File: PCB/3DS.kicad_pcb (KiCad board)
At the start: 2 copper layers, 12 x 40.6 mm, 8 parts, among them J1 3DS Joystick Pads, U1 ATtiny45V-10SU

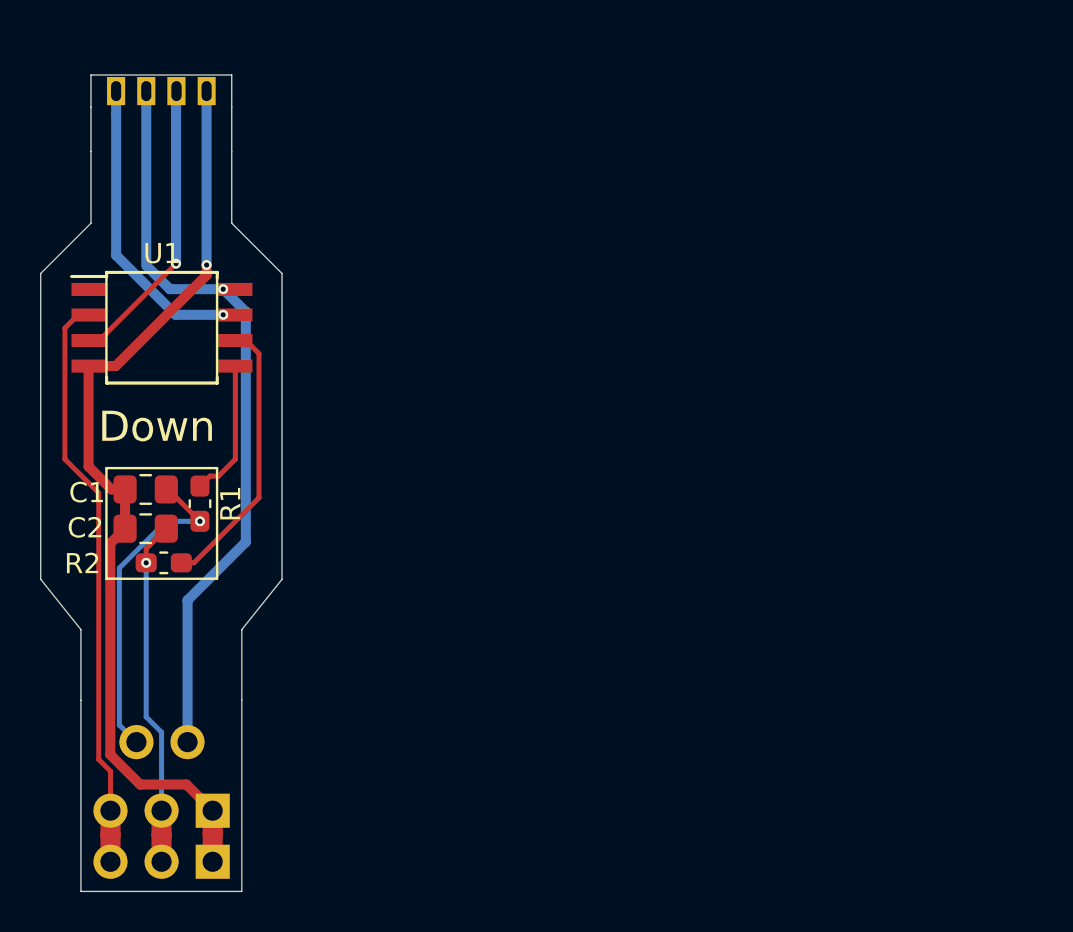
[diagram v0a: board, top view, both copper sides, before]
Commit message: Moved from flex PCB to a roughed-out fiberglass PCB
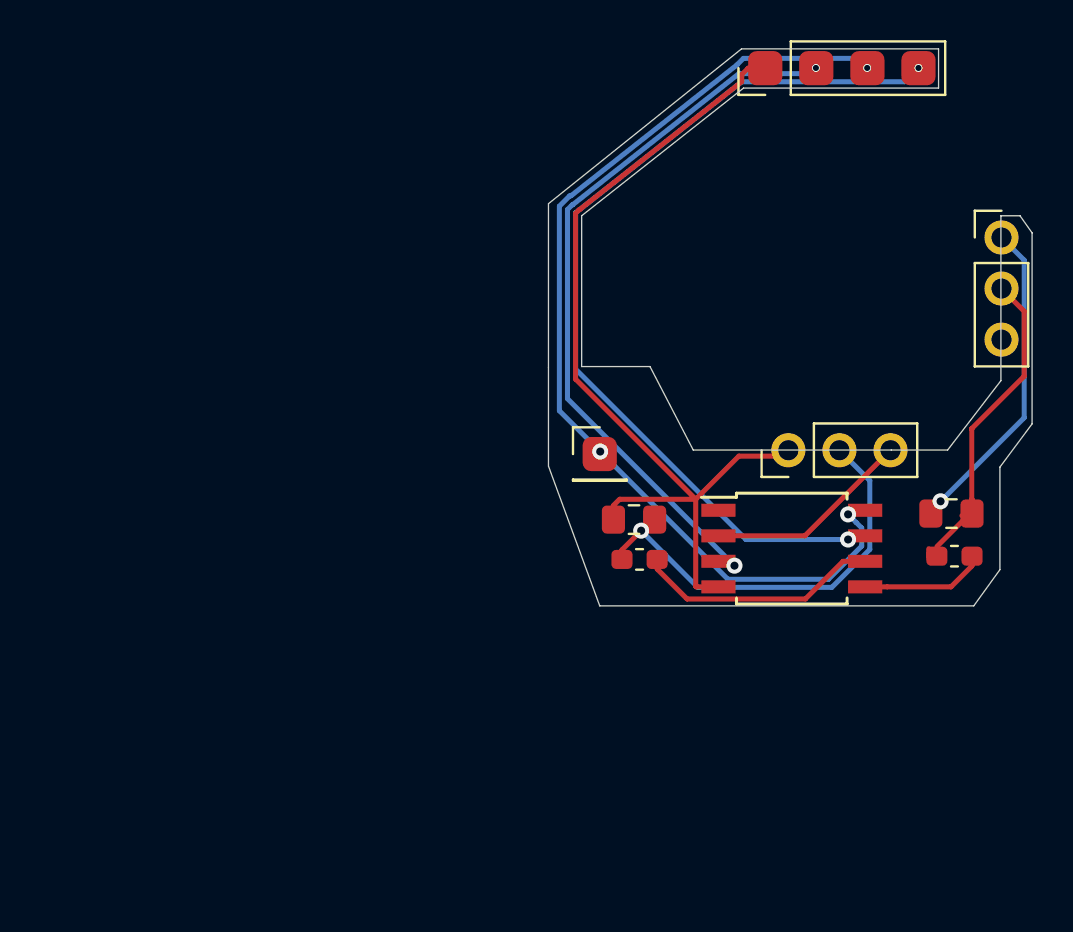
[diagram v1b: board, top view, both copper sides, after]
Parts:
- removed  : PinHeader_2x01_P2.54mm_Vertical, Connector_PinHeader_2.54mm:PinHeader_2x01_P2.54mm_Vertical
- removed J1: 3DS Joystick Pads, Custom Footprints:3DS_Joypad
- removed XB1: PinHeader_2x03_P2.54mm_Vertical, Connector_PinHeader_2.54mm:PinHeader_2x03_P2.54mm_Vertical
- added REF**: PinHeader_1x04_P2.54mm_Vertical, Connector_PinHeader_2.54mm:PinHeader_1x04_P2.54mm_Vertical, F.Cu at (102.5, 38.7)
- added REF**: PinHeader_1x03_P2.54mm_Vertical, Connector_PinHeader_2.54mm:PinHeader_1x03_P2.54mm_Vertical, F.Cu at (114.3, 47.1)
- added REF**: PinHeader_1x03_P2.54mm_Vertical, Connector_PinHeader_2.54mm:PinHeader_1x03_P2.54mm_Vertical, F.Cu at (103.7, 57.7)
- added \: PinHeader_1x01_P2.54mm_Vertical, Connector_PinHeader_2.54mm:PinHeader_1x01_P2.54mm_Vertical, F.Cu at (94.3, 57.9)
- moved C1 40.1 mm to (111.8, 60.8)
- moved R1 37.6 mm to (111.9, 62.9), turned to 0 degrees
- moved U1 33.2 mm to (103.8, 62.5)
- moved C2 24.3 mm to (96.0, 61.1)
- moved R2 23.7 mm to (96.3, 63.1)
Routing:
- net Xin: track 15.1 -> 44.4 mm, vias 1 -> 2
- net YIn: track 14.6 -> 36.0 mm, vias 1 -> 2
- net StickReference: track 28.9 -> 10.2 mm
- net GND: track 47.0 -> 60.0 mm
- net +3V3: track 37.7 -> 49.3 mm, vias 1 -> 3
- net XOut: track 17.3 -> 21.5 mm
- net Net-(R2-Pad2): track 13.8 -> 12.2 mm
- net YOut: track 16.3 -> 15.5 mm, vias 1 -> 0
- net Net-(R1-Pad2): track 6.95 -> 6.22 mm
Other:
- board size 12 x 40.6 mm -> 24 x 27.7 mm
- net class Default: clearance 0.2 -> 0.1524
- rule pad_to_mask_clearance: 0.0762 -> 0.0508
- rule solder_mask_min_width: 0.1016 -> 0.101
- rule trace_clearance: 0.2 -> 0.1524
- rule trace_min: 0.2 -> 0.1524
- rule via_min_drill: 0.3 -> 0.254
- rule via_min_size: 0.4 -> 0.127
- board text removed: "3.3V"
- board text removed: "Down"
- board text removed: "Y"
